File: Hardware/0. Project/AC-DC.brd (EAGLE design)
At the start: 100 x 75 mm, 100 parts, among them IC4 LM358D, IC5 LM393D, IC6 LM393D, K1 12VDC COIL, K2 12VDC COIL, K3 12VDC COIL, K4 12VDC COIL, Q1 BC848SMD, Q2 BC848BSMD, Q3 BC858BSMD, Q4 BC858BSMD, Q6 BC858BSMD, Q7 BC848SMD, U1 LM338K, U2 LM338K, U3 HLK-PM01

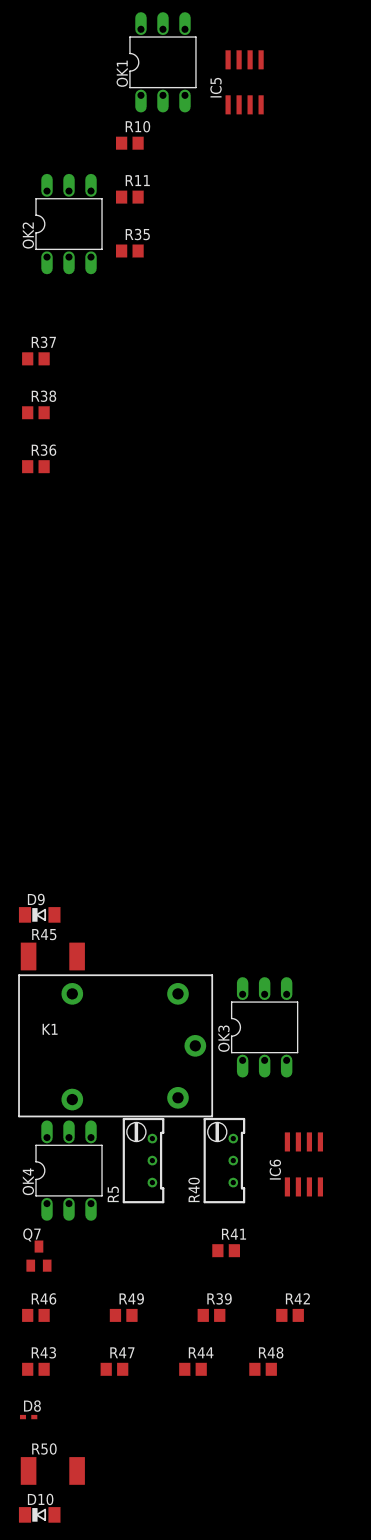
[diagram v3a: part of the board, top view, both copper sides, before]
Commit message: Schematic 2.0 done
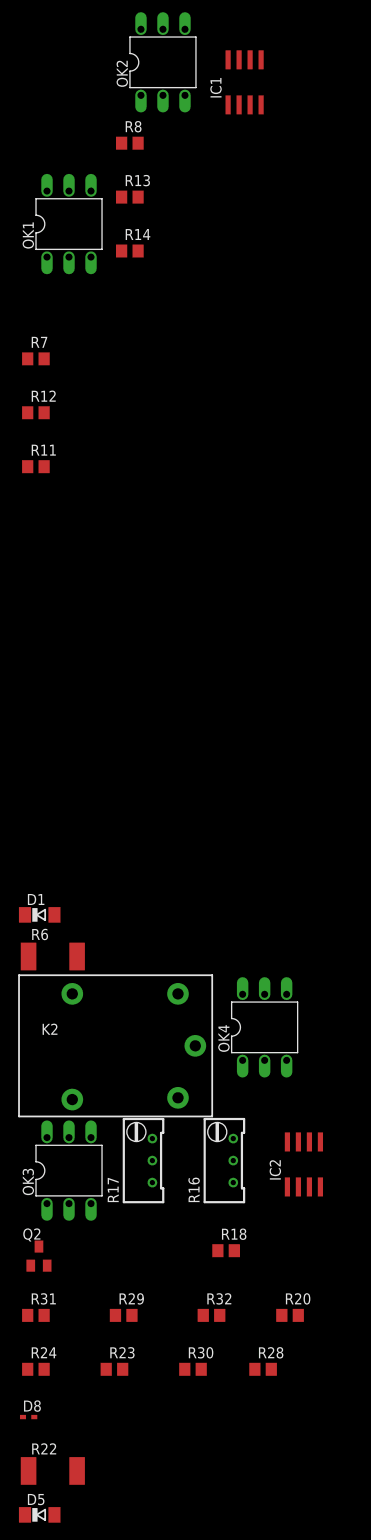
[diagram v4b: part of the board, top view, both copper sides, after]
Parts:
- removed C12: 15.000uF x 50V, rcl:EB35D
- removed C13: 100nF x 50V, rcl:C0805
- removed C14: 10uF x 50V, rcl:153CLV-0605
- removed Q7: BC848SMD, transistor-npn:SOT23
- removed R3: 100k (1%), rcl:R0805
- removed R46, R49: 100k (5%), rcl:R0805
- removed R47: 10k (5%), rcl:R0805
- removed R48: 1k (5%), rcl:R0805
- removed RT4: 5R, ptc-ntc:11MM
- added C1: 15.000uF x 50V, rcl:EB35D
- added C2: 100nF x 50V, rcl:C0805
- added C3: 10uF x 50V, rcl:153CLV-0605
- added Q5: BC858, transistor-pnp:SOT23-BEC
- added R15, R32: 10k (5%), rcl:R0805
- added R17, R2: 500k, rcl:RTRIM64W
- added R30: 1k (5%), rcl:R0805
- added RT3: 10k, ptc-ntc:MOLEX2P
- D1: value 1N4148 -> 12V / 0.5W; device diode:SOD523 -> diode:SOD80C
- D10, D9: value (none) -> 1N4148; device diode:SOD80C -> diode:SOD523
- D4: value 1N4007 -> 1N4148; device diode:SOD-123_MINI-SMA -> diode:SOD523
- D5: value 1N4007 -> 12V / 0.5W; device diode:SOD-123_MINI-SMA -> diode:SOD80C
- D6, D7: value 1N4148 -> 1N4007; device diode:SOD523 -> diode:SOD-123_MINI-SMA
- Q1: value BC848SMD -> BC848
- Q2: value BC848BSMD -> BC848
- Q3, Q6: value BC858BSMD -> BC858
- Q4: value BC858BSMD -> BC848; device transistor-pnp:SOT23-BEC -> transistor-npn:SOT23
- R10: value 10k (5%) -> 5K; device rcl:R0805 -> trimpot-molex2p:MOLEX3P
- R12: value 33k (5%) -> 100k (5%)
- R13: value 500R -> 1k (5%); device rcl:RTRIM64W -> rcl:R0805
- R14: value 5K -> 100k (5%); device trimpot-molex2p:MOLEX3P -> rcl:R0805
- R16: value 10k (5%) -> 500k; device rcl:R0805 -> rcl:RTRIM64W
- R19, R21: value 100k (1%) -> 10k; device rcl:R0805 -> rcl:RTRIM64W
- R20: value 100k (1%) -> 33k (1%)
- R22: value (none) -> 220R
- R23: value 220k (5%) -> 10k (5%)
- R25: value 1k (5%) -> 33k (5%)
- R28, R34: value 10k (5%) -> 1k (5%)
- R29, R44: value 1k (5%) -> 100k (5%)
- R31: value 10k (5%) -> 100k (5%)
- R33, R35: value 100k (5%) -> 10k (5%)
- R37: value 10k (5%) -> 100k (1%)
- R38: value 100k (5%) -> 100k (1%)
- R4: value 33k (1%) -> 100k (1%)
- R40: value 500k -> 100k (1%); device rcl:RTRIM64W -> rcl:R0805
- R42: value 33k (1%) -> 10k (5%)
- R43: value 10k (5%) -> 220k (5%)
- R45: value (none) -> 10k (5%); device rcl:R2512 -> rcl:R0805
- R5: value 500k -> 33k (1%); device rcl:RTRIM64W -> rcl:R0805
- R6: value 10k (5%) -> 220R; device rcl:R0805 -> rcl:R2512
- R7: value 500k -> 10k (5%); device rcl:RTRIM64W -> rcl:R0805
- R8: value 10k -> 10k (5%); device rcl:RTRIM64W -> rcl:R0805
- R9: value 10k -> 500R
- RT2: value 10k -> 5R; device ptc-ntc:MOLEX2P -> ptc-ntc:11MM
- U2: value LM338K -> HLK-PM01; device REG1117:MOLEX3P -> HLK-PM01:HLK-PM01
- U3: value HLK-PM01 -> LM338K; device HLK-PM01:HLK-PM01 -> REG1117:MOLEX3P
- moved D5 289.4 mm to (-40.6, -197.4), flipped to the top, turned to 0 degrees
- moved D10 272.3 mm to (89.4, 41.9), flipped to the bottom
- moved R24 254.8 mm to (-41.1, -180.6), flipped to the top, turned to 0 degrees
- moved R29 247.1 mm to (-30.9, -174.3), flipped to the top, turned to 0 degrees
- moved R43 243.8 mm to (52.7, 44.6), flipped to the bottom, turned to 270 degrees
- moved R31 243.4 mm to (-41.1, -174.3), flipped to the top, turned to 0 degrees
- moved R23 240.5 mm to (-32.0, -180.6), flipped to the top, turned to 0 degrees
- moved R44 240.3 mm to (86.9, 33.2), flipped to the bottom, turned to 90 degrees
- moved R28 237.0 mm to (-14.8, -180.6), flipped to the top, turned to 0 degrees
- moved Q2 236.1 mm to (-40.7, -167.5), flipped to the top
- moved R20 233.6 mm to (-11.7, -174.3), flipped to the top, turned to 0 degrees
- moved R39 233.6 mm to (72.9, 39.6), flipped to the bottom, turned to 90 degrees
- moved R42 230.9 mm to (75.1, 39.6), flipped to the bottom, turned to 90 degrees
- moved R41 226.4 mm to (49.6, 48.8), flipped to the bottom, turned to 270 degrees
- moved R18 225.7 mm to (-19.1, -166.9), flipped to the top, turned to 0 degrees
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- renumbered C11 to C4, C15 to C10, IC4 to IC3, IC5 to IC1, IC6 to IC2, R50 to R22
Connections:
- removed net HIGH_TEMPERATURE_1: R28.1, R31.1
- net !SHORT_CIRCUIT_DETECTED!: now also OK2.4, OK4.4, Q4.3, R14.2, R31.2; no longer OK1.4, OK3.4, Q2.3, R35.2, R46.2
- net !VOUT1_POWER_OFF!: now also R34.2, R35.1, R43.2, R44.1, R45.1; no longer R16.1, R23.2, R25.2, R33.1, R34.1
- net !VOUT1_POWER_ON!: now also R33.2, R37.1, R38.2; no longer R18.1, R19.2, R24.2
- net !VOUT1_POWER_ON!1: now also OK2.5, R13.1; no longer OK1.5, R11.1
- net !VOUT1_POWER_ON!2: now also OK1.5, R11.1; no longer OK2.5, R36.1
- net !VOUT1_POWER_ON!3: now also OK4.5, R30.1; no longer OK3.5, R44.1
- net !VOUT1_POWER_ON!4: now also OK3.5, R28.1; no longer OK4.5, R48.1
- net +12V: now also D4.C, Q5.E, R13.2, R19.3, R30.2, R37.2, R39.2, R40.2, RT3.P$2, U2.P$4; no longer D1.C, Q4.E, R18.2, R20.2, R36.2, R44.2, R48.2, R8.3, RT2.P$2, U3.P$4
- net 0V_B: now also U2.P$2; no longer U3.P$2
- net 127V_B: now also U2.P$1; no longer U3.P$1
- net 12V_AUX1: now also D1.C, R2.3, R6.1; no longer D9.C, R45.1, R7.3
- net 12V_AUX2: now also D5.C, R16.3, R17.3; no longer D10.C, R40.3, R5.3
- net C_FULL_1: now also C1.+, C2.1, K1.14, R4.2, R6.2; no longer C7.+, C8.1, K2.14, R3.2, R45.2
- net C_FULL_2: now also C7.+, C8.1, D6.C, K2.14, R18.2, RT2.P$1, U3.1; no longer C12.+, C13.1, D4.C, K1.14, R41.2, RT4.P$1, U2.1
- net GND1: now also C1.-, C2.2, C3.-, D1.A, R10.P$1, R10.P$3, R2.1, R5.1; no longer C7.-, C8.2, C9.-, D9.A, R14.P$1, R14.P$3, R33.2, R4.1, R7.1
- net GND2: now also C7.-, C8.2, C9.-, D5.A, R16.1, R17.1, R20.1; no longer C12.-, C13.2, C14.-, D10.A, R40.1, R42.1, R5.1
- net HIGH_TEMPERATURE: now also R25.2, R39.1, R42.1; no longer R12.2
- net N$1: now also K1.11; no longer K2.11
- net N$12: now also D10.C, R36.1; no longer D7.C, R29.1
- net N$13: now also R36.2; no longer R29.2
- net N$14: now also R33.1; no longer R24.1
- net N$15: now also R9.3; no longer R13.3
- net N$16: now also C3.+, R10.P$2, R9.1, R9.2; no longer C9.+, R13.1, R13.2, R14.P$2
- net N$18: now also R4.1, R5.2; no longer R3.1, R4.2
- net N$19: now also R8.1; no longer R10.1
- net N$2: now also D4.A, K1.A2; no longer D1.A, K2.A2
- net N$20: now also OK2.1, R8.2; no longer OK1.1, R10.2
- net N$21: now also Q4.2, R40.1, R41.2, R43.1; no longer Q2.2, R20.1, R21.2, R23.1
- net N$22: now also Q4.1, R35.2; no longer Q2.1, R16.2
- net N$25: now also R2.2; no longer R7.2
- net N$26: now also D6.A, D7.C, U3.3; no longer D4.A, D5.C, U2.3
- net N$27: now also C9.+, D7.A, U3.2; no longer C14.+, D5.A, U2.2
- net N$29: now also K2.11, RT2.P$2; no longer K1.11, RT4.P$2
- net N$3: now also R34.1; no longer R25.1
- net N$32: now also Q5.B, R42.2; no longer Q4.B, R31.2
- net N$33: now also K2.A2, Q2.3; no longer K1.A2, Q7.3
- net N$35: now also R21.2, R21.3, RT3.P$1; no longer R9.2, R9.3, RT2.P$1
- net N$36: now also R19.2, R25.1; no longer R12.1, R8.2
- net N$37: now also R7.1; no longer R37.1
- net N$38: now also D9.C, Q5.C; no longer D6.C, Q4.C
- net N$39: now also OK1.1, R7.2; no longer OK2.1, R37.2
- net N$4: now also R15.2; no longer R6.2
- net N$40: now also Q2.1, R32.2; no longer Q7.1, R39.2
- net N$41: now also R18.1, R20.2; no longer R41.1, R42.2
- net N$42: now also R24.1; no longer R43.1
- net N$43: now also R16.2; no longer R40.2
- net N$44: now also OK4.1, R24.2; no longer OK3.1, R43.2
- net N$45: now also R23.1; no longer R47.1
- net N$46: now also OK3.1, R23.2; no longer OK4.1, R47.2
- net N$47: now also OK3.4, R29.2, R32.1; no longer OK4.4, R39.1, R49.2
- net N$48: now also OK1.4, R12.2, R15.1; no longer OK2.4, R38.2, R6.1
- net N$5: now also R17.2; no longer R5.2
- net N$7: now also R45.2; no longer R34.2
- net PE: now also D10.A, D9.A, Q2.2, R12.1, R14.1, R29.1, R31.1, R41.1, R44.2, U2.P$3; no longer D6.A, D7.A, Q7.2, R35.1, R46.1, R49.1, R8.1, R9.1, U3.P$3

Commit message: Schematic 2.1 (better organization)
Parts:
- added C11, C12, C15: 100nF x 50V, rcl:C0805
- added C13, C14: 10uF x 50V, rcl:153CLV-0605
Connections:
- removed net +24V: VOLT1.P$1, VOLT2.P$1
- new net 0V: C11.2, C12.2
- net +12V: now also C15.1
- net 12V_AUX1: now also C11.1, C13.+, VOLT1.P$1
- net 12V_AUX2: now also C12.1, C14.+, VOLT2.P$1
- net GND1: now also C13.-
- net GND2: now also C14.-
- net PE: now also C15.2
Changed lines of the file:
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@@
 <attribute name="VALUE" x="-41.656" y="-195.4657" size="1.27" layer="27"/>
+</element>
+<element name="C11" library="rcl" library_urn="urn:adsk.eagle:library:334" package="C0805" package3d_urn="urn:adsk.eagle:package:23617/2" value="100nF x 50V" x="-41.0718" y="-203.4032" smashed="yes">
+<attribute name="NAME" x="-42.3418" y="-202.1332" size="1.27" layer="25"/>
+<attribute name="POPULARITY" value="88" x="-41.0718" y="-203.4032" size="1.778" layer="27" display="off"/>
+<attribute name="SPICEPREFIX" value="C" x="-41.0718" y="-203.4032" size="1.778" layer="27" display="off"/>
+<attribute name="VALUE" x="-42.3418" y="-205.9432" size="1.27" layer="27"/>
+</element>
+<element name="C12" library="rcl" library_urn="urn:adsk.eagle:library:334" package="C0805" package3d_urn="urn:adsk.eagle:package:23617/2" value="100nF x 50V" x="-41.0718" y="-209.6262" smashed="yes">
+<attribute name="NAME" x="-42.3418" y="-208.3562" size="1.27" layer="25"/>
+<attribute name="POPULARITY" value="88" x="-41.0718" y="-209.6262" size="1.778" layer="27" display="off"/>
+<attribute name="SPICEPREFIX" value="C" x="-41.0718" y="-209.6262" size="1.778" layer="27" display="off"/>
+<attribute name="VALUE" x="-42.3418" y="-212.1662" size="1.27" layer="27"/>
+</element>
+<element name="C13" library="rcl" library_urn="urn:adsk.eagle:library:334" package="153CLV-0605" package3d_urn="urn:adsk.eagle:package:23398/2" value="10uF x 50V" x="-47.7393" y="-207.2259" smashed="yes">
+<attribute name="NAME" x="-51.1293" y="-203.5959" size="1.27" layer="25"/>
+<attribute name="POPULARITY" value="5" x="-47.7393" y="-207.2259" size="1.778" layer="27" display="off"/>
+<attribute name="SPICEPREFIX" value="C" x="-47.7393" y="-207.2259" size="1.778" layer="27" display="off"/>
+<attribute name="VALUE" x="-51.1643" y="-212.1109" size="1.27" layer="27"/>
+</element>
+<element name="C14" library="rcl" library_urn="urn:adsk.eagle:library:334" package="153CLV-0605" package3d_urn="urn:adsk.eagle:package:23398/2" value="10uF x 50V" x="-56.896" y="-207.2259" smashed="yes">
+<attribute name="NAME" x="-60.286" y="-203.5959" size="1.27" layer="25"/>
+<attribute name="POPULARITY" value="5" x="-56.896" y="-207.2259" size="1.778" layer="27" display="off"/>
+<attribute name="SPICEPREFIX" value="C" x="-56.896" y="-207.2259" size="1.778" layer="27" display="off"/>
+<attribute name="VALUE" x="-60.321" y="-212.1109" size="1.27" layer="27"/>
+</element>
+<element name="C15" library="rcl" library_urn="urn:adsk.eagle:library:334" package="C0805" package3d_urn="urn:adsk.eagle:package:23617/2" value="100nF x 50V" x="-59.3852" y="-215.8492" smashed="yes">
+<attribute name="NAME" x="-60.6552" y="-214.5792" size="1.27" layer="25"/>
+<attribute name="POPULARITY" value="88" x="-59.3852" y="-215.8492" size="1.778" layer="27" display="off"/>
+<attribute name="SPICEPREFIX" value="C" x="-59.3852" y="-215.8492" size="1.778" layer="27" display="off"/>
+<attribute name="VALUE" x="-60.6552" y="-218.3892" size="1.27" layer="27"/>
 </element>
 </elements>
@@
 <wire x1="-15.0749" y1="-29.404" x2="52.6796" y2="31.2522" width="0" layer="19" extent="1-16"/>
 </signal>
-<signal name="+24V">
-<contactref element="VOLT1" pad="P$1"/>
-<contactref element="VOLT2" pad="P$1"/>
-<via x="74.3458" y="37.1348" extent="1-16" drill="0.35"/>
-<via x="71.7804" y="44.8056" extent="1-16" drill="0.35"/>
-<wire x1="71.7804" y1="44.8056" x2="96" y2="72.5" width="0" layer="19" extent="1-1"/>
-<wire x1="74.3458" y1="37.1348" x2="71.7804" y2="44.8056" width="0" layer="19" extent="1-1"/>
-<wire x1="96" y1="7.415" x2="74.3458" y2="37.1348" width="0" layer="19" extent="1-1"/>
-</signal>
 <signal name="VOUT_2">
 <contactref element="K3" pad="11"/>
@@
 <contactref element="IC3" pad="8"/>
 <contactref element="RT3" pad="P$2"/>
+<contactref element="C15" pad="1"/>
 <wire x1="-21.9862" y1="-180.5559" x2="-42.5608" y2="-186.0677" width="0" layer="19" extent="1-1"/>
 <wire x1="-13.8963" y1="-180.5559" x2="-21.9862" y2="-180.5559" width="0" layer="19" extent="1-1"/>
+<wire x1="-60.3352" y1="-215.8492" x2="-42.5608" y2="-186.0677" width="0" layer="19" extent="1-1"/>
 <wire x1="-24.6695" y1="-137.2179" x2="-21.9862" y2="-180.5559" width="0" layer="19" extent="1-1"/>
 <wire x1="-40.1218" y1="-76.3651" x2="-24.6695" y2="-137.2179" width="0" layer="19" extent="1-1"/>
@@
 <contactref element="OK1" pad="2"/>
 <contactref element="OK2" pad="2"/>
+<contactref element="C13" pad="-"/>
 <wire x1="95.8342" y1="64.5414" x2="98.4504" y2="73.3806" width="0" layer="19" extent="1-1"/>
 <wire x1="97.409" y1="62.3062" x2="95.8342" y2="64.5414" width="0" layer="19" extent="1-1"/>
@@
 <wire x1="-37.2491" y1="-52.1716" x2="-26.4033" y2="-33.5026" width="0" layer="19" extent="1-1"/>
 <wire x1="-38.9273" y1="-128.1049" x2="-37.2491" y2="-52.1716" width="0" layer="19" extent="1-1"/>
+<wire x1="-50.4393" y1="-207.2259" x2="-38.9273" y2="-128.1049" width="0" layer="19" extent="1-1"/>
 </signal>
 <signal name="N$6">
@@
 <contactref element="IC3" pad="4"/>
 <contactref element="R44" pad="2"/>
+<contactref element="C15" pad="2"/>
 <wire x1="-39.7662" y1="-168.5876" x2="-42.0218" y2="-174.3329" width="0" layer="19" extent="1-1"/>
 <wire x1="-31.8872" y1="-174.3329" x2="-39.7662" y2="-168.5876" width="0" layer="19" extent="1-1"/>
+<wire x1="-58.4352" y1="-215.8492" x2="-42.0218" y2="-174.3329" width="0" layer="19" extent="1-1"/>
 <wire x1="-42.0218" y1="-70.1421" x2="-39.7662" y2="-168.5876" width="0" layer="19" extent="1-1"/>
 <wire x1="-31.176" y1="-51.4731" x2="-42.0218" y2="-70.1421" width="0" layer="19" extent="1-1"/>
@@
 <contactref element="IC1" pad="8"/>
 <contactref element="R2" pad="3"/>
+<contactref element="VOLT1" pad="P$1"/>
+<via x="74.3458" y="37.1348" extent="1-16" drill="0.35"/>
+<via x="71.7804" y="44.8056" extent="1-16" drill="0.35"/>
+<contactref element="C11" pad="1"/>
+<contactref element="C13" pad="+"/>
+<wire x1="-42.0218" y1="-203.4032" x2="-45.0393" y2="-207.2259" width="0" layer="19" extent="1-1"/>
+<wire x1="-41.916" y1="-132.9055" x2="-42.0218" y2="-203.4032" width="0" layer="19" extent="1-1"/>
 <wire x1="-42.3273" y1="-128.1049" x2="-41.916" y2="-132.9055" width="0" layer="19" extent="1-1"/>
 <wire x1="-18.8849" y1="-29.404" x2="-42.3273" y2="-128.1049" width="0" layer="19" extent="1-1"/>
 <wire x1="20.193" y1="40.1066" x2="-18.8849" y2="-29.404" width="0" layer="19" extent="1-1"/>
 <wire x1="44.1706" y1="40.4622" x2="20.193" y2="40.1066" width="0" layer="19" extent="1-1"/>
+<wire x1="71.7804" y1="44.8056" x2="44.1706" y2="40.4622" width="0" layer="19" extent="1-1"/>
+<wire x1="74.3458" y1="37.1348" x2="71.7804" y2="44.8056" width="0" layer="19" extent="1-1"/>
+<wire x1="96" y1="7.415" x2="74.3458" y2="37.1348" width="0" layer="19" extent="1-1"/>
 </signal>
 <signal name="N$5">
@@
 <contactref element="R16" pad="3"/>
 <contactref element="R17" pad="3"/>
+<contactref element="VOLT2" pad="P$1"/>
+<contactref element="C12" pad="1"/>
+<contactref element="C14" pad="+"/>
+<wire x1="-42.3273" y1="-197.358" x2="-42.0218" y2="-209.6262" width="0" layer="19" extent="1-1"/>
 <wire x1="-41.916" y1="-192.2907" x2="-42.3273" y2="-197.358" width="0" layer="19" extent="1-1"/>
+<wire x1="-54.196" y1="-207.2259" x2="-42.0218" y2="-209.6262" width="0" layer="19" extent="1-1"/>
 <wire x1="-27.6225" y1="-153.924" x2="-41.916" y2="-192.2907" width="0" layer="19" extent="1-1"/>
 <wire x1="-18.288" y1="-153.924" x2="-27.6225" y2="-153.924" width="0" layer="19" extent="1-1"/>
 <wire x1="-12.0396" y1="-154.3085" x2="-18.288" y2="-153.924" width="0" layer="19" extent="1-1"/>
+<wire x1="96" y1="72.5" x2="-12.0396" y2="-154.3085" width="0" layer="19" extent="1-1"/>
 </signal>
 <signal name="GND2">
@@
 <contactref element="D5" pad="A"/>
 <contactref element="OK4" pad="2"/>
+<contactref element="C14" pad="-"/>
+<wire x1="-59.596" y1="-207.2259" x2="-38.9273" y2="-197.358" width="0" layer="19" extent="1-1"/>
 <wire x1="-12.6848" y1="-174.3329" x2="-38.9273" y2="-197.358" width="0" layer="19" extent="1-1"/>
 <wire x1="-8.2296" y1="-159.5085" x2="-12.6848" y2="-174.3329" width="0" layer="19" extent="1-1"/>
@@
 <wire x1="64.8564" y1="30.3784" x2="65.151" y2="32.9692" width="0" layer="19" extent="16-16"/>
 </signal>
+<signal name="0V">
+<contactref element="C11" pad="2"/>
+<contactref element="C12" pad="2"/>
+<wire x1="-40.1218" y1="-203.4032" x2="-40.1218" y2="-209.6262" width="0" layer="19" extent="1-1"/>
+</signal>
 </signals>

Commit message: Working on at 2.1 schematic
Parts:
- added D11: 1N4148, diode:SOD80C
- added X3: (no value), con-molex-PTR:22-23-2021
- D10, D4, D8, D9: device diode:SOD523 -> diode:SOD80C
- K1, K2, K3, K4: device relay:ZN5 -> relay:CQ1
- OK1, OK2, OK3, OK4: device optocoupler:DIL06 -> optocoupler:DIL6-SMD
- R26, R9: device rcl:RTRIM64W -> pot:CA6V
- moved R20 259.4 mm to (-145.4, 48.0), flipped to the bottom
- moved R18 252.1 mm to (-138.0, 55.5), flipped to the bottom
- moved D8 252.1 mm to (27.4, 56.3), flipped to the bottom, turned to 270 degrees
- moved C13 243.7 mm to (69.9, 6.22), flipped to the bottom, turned to 270 degrees
- moved IC2 241.1 mm to (-90.8, 70.3), flipped to the bottom, turned to 90 degrees
- moved R23 241.0 mm to (-125.1, 41.8), flipped to the bottom
- moved R22 235.9 mm to (-118.0, 30.0), flipped to the bottom
- moved D5 234.9 mm to (-116.5, 25.0), flipped to the bottom
- moved C12 234.6 mm to (-116.0, 12.7), flipped to the bottom
- moved R24 234.6 mm to (-116.0, 41.8), flipped to the bottom
- moved C11 234.6 mm to (-116.0, 18.9), flipped to the bottom
- moved C14 226.5 mm to (-100.2, 15.1), flipped to the bottom
- moved C15 225.6 mm to (-97.7, 6.49), flipped to the bottom
- moved R16 214.8 mm to (90.9, 27.8), turned to 90 degrees
- moved R17 214.3 mm to (80.5, 27.8), turned to 90 degrees
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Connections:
- net !VOUT1_POWER_OFF! renamed !VOUT_POWER_OFF!
- net +12V: now also K1.1, K2.1; no longer K1.A1, K2.A1
- net 0V_B: now also X3.2
- net 127V_B: now also X3.1
- net C_FULL_1: now also K1.NO; no longer K1.14
- net C_FULL_2: now also K2.NO; no longer K2.14
- net N$1: now also K1.C; no longer K1.11
- net N$12: now also D11.C, K3.1, K4.1; no longer K3.A1, K4.A1
- net N$15: now also R9.E; no longer R9.3
- net N$16: now also R9.A, R9.S; no longer R9.1, R9.2
- net N$17: now also K4.NC; no longer K4.12
- net N$2: now also K1.2; no longer K1.A2
- net N$26: now also R26.E; no longer R26.3
- net N$27: now also R26.A, R26.S; no longer R26.1, R26.2
- net N$28: now also K3.NC; no longer K3.12
- net N$29: now also K2.C; no longer K2.11
- net N$33: now also K2.2; no longer K2.A2
- net PE: now also D11.A, K3.2, K4.2; no longer K3.A2, K4.A2
- net VOUT_1: now also K4.C; no longer K4.11
- net VOUT_2: now also K3.C; no longer K3.11
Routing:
- net GND1: track 9.97 -> 97.0 mm, vias 132 -> 0
- net N$15: track 107.1 -> 54.8 mm
- net N$1: track 62.5 -> 14.1 mm
- net N$26: track 100.9 -> 53.1 mm
- net C_FULL_1: track 74.1 -> 38.6 mm
- net PE: track 33.9 -> 0.00 mm
- net C_FULL_2: track 57.7 -> 25.9 mm
- net VOUT_1: track 52.6 -> 20.9 mm, vias 1 -> 0
- net N$10: track 38.9 -> 18.6 mm
- net N$24: track 0.00 -> 18.3 mm
- net GND2: track 112.9 -> 95.9 mm
- net N$23: track 21.6 -> 7.59 mm
- net N$17: track 20.1 -> 7.36 mm
- net N$28: track 19.7 -> 7.62 mm
- net N$29: track 24.5 -> 13.5 mm
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- removed copper zone on layer 1, net GND1
- removed copper zone on layer 16, net GND1
